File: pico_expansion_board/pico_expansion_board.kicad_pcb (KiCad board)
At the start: 4 copper layers, 99.1 x 69.8 mm, 55 parts, among them J1 DC12V/24V, J10 CAN_L, J2 TMC2209 Motor 1, J3 TMC2209 Motor 2, J4 Motor 1, J5 Motor 2, J6 A&D FX DB9_INV, J7 A&D FX DB9, J8 EXP1, J9 EXP2, SW1 SW_Push, U1 MAX232, U2 MCP2542FDxMF, U3 Pico, U4 AT24CS08-XHM, U5 TPS5450DDAR

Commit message: Update design
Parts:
- removed C10, C11: 4.7uF, Capacitor_SMD:C_0805_2012Metric
- removed C12, C13, C15: 0.01uF, Capacitor_SMD:C_0805_2012Metric
- removed C14: 220uF, Capacitor_SMD:CP_Elec_10x10.5
- removed D3: SS54, SnapEDAFootPrint:DO-214AC
- removed JP5: TX_OP2, Connector_PinHeader_2.54mm:PinHeader_1x02_P2.54mm_Vertical
- removed JP6: RX_OP2, Connector_PinHeader_2.54mm:PinHeader_1x02_P2.54mm_Vertical
- removed JP7: TX_OP1, Connector_PinHeader_2.54mm:PinHeader_1x02_P2.54mm_Vertical
- removed JP8: RX_OP1, Connector_PinHeader_2.54mm:PinHeader_1x02_P2.54mm_Vertical
- removed L2: 15uH, Inductor_SMD:L_Vishay_IHLP-4040
- removed R4: 10K, Resistor_SMD:R_0805_2012Metric
- removed R5: 3.16K, Resistor_SMD:R_0805_2012Metric
- removed TP3: TestPoint, TestPoint:TestPoint_Pad_2.0x2.0mm
- removed U5: TPS5450DDAR, SnapEDAFootPrint:CONV_TPS5450DDAR
- added C16: 10nF, Capacitor_SMD:C_0805_2012Metric, F.Cu at (130.0, 113.5)
- added C17: 10nF, Capacitor_SMD:C_0805_2012Metric, F.Cu at (120.1, 108.2)
- added C18: 330uF, Capacitor_SMD:CP_Elec_10x10.5, F.Cu at (115.3, 101.3)
- added C19: 10nF, Capacitor_SMD:C_0805_2012Metric, F.Cu at (125.0, 96.8)
- added C5: 4.7uF, Capacitor_SMD:C_0805_2012Metric, F.Cu at (124.5, 113.5)
- added C9: 4.7uF, Capacitor_SMD:C_0805_2012Metric, F.Cu at (127.3, 113.5)
- added D1: SS54, Extra Footprints:DO-214AC, F.Cu at (114.8, 108.2)
- added IC1: TPS5450DDA, Extra Footprints:SOIC127P600X170-9N, F.Cu at (119.1, 112.5)
- added L1: 15uH, Inductor_SMD:L_10.4x10.4_H4.8, F.Cu at (128.8, 104.9)
- added R2: 10K, Resistor_SMD:R_0805_2012Metric, F.Cu at (111.8, 112.3)
- added R6: 3.16K, Resistor_SMD:R_0805_2012Metric, F.Cu at (114.0, 112.3)
- added TP6: TestPoint, TestPoint:TestPoint_Pad_2.0x2.0mm, F.Cu at (133.9, 116.1)
- C2, C3: value 0.1uF -> 100nF
- C4: value 0.1uF -> 1uF
- H1, H2, H3, H4: footprint MountingHole:MountingHole_3.2mm_M3_Pad_Via -> MountingHole:MountingHole_3.2mm_M3_Pad
- J6: value A&D FX DB9_INV -> Straight Through
- J7: value A&D FX DB9 -> NULL Modem
- JP1, JP2: footprint Connector_PinHeader_2.54mm:PinHeader_1x02_P2.54mm_Vertical -> Connector_PinHeader_2.00mm:PinHeader_1x02_P2.00mm_Vertical
- JP3, JP4: footprint Connector_PinHeader_2.54mm:PinHeader_1x02_P2.54mm_Vertical -> Connector_PinSocket_2.00mm:PinSocket_1x02_P2.00mm_Vertical
- JP9: value TX_OP2 -> 120JP; footprint Connector_PinHeader_2.54mm:PinHeader_1x02_P2.54mm_Vertical -> Connector_PinHeader_2.00mm:PinHeader_1x02_P2.00mm_Vertical
- R1: value 10K -> 120Ω
- moved TP2 5.80 mm to (129.3, 86.1)
- moved TP8 3.07 mm to (68.8, 63.8)
- moved TP7 1.98 mm to (74.9, 63.8)
- moved TP1 1.21 mm to (129.3, 80.8), turned to -90 degrees
- moved JP2 0.52 mm to (70.3, 78.7)
- moved JP4 0.52 mm to (70.3, 105.9)
- moved JP9 0.36 mm to (114.6, 73.4)
- moved TP5 0.25 mm to (89.2, 102.9)
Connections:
- J6 pad 2: Net-(JP5-B) -> SCALE_RXD
- J6 pad 3: Net-(JP6-A) -> SCALE_TXD
- J7 pad 2: Net-(JP7-B) -> SCALE_TXD
- J7 pad 3: Net-(JP8-A) -> SCALE_RXD
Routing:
- net SCALE_TXD: track 19.5 -> 55.7 mm
- net Net-(JP6-A): track 28.8 -> 0.00 mm
- net Net-(JP5-B): track 28.5 -> 0.00 mm
- net SCALE_RXD: track 34.1 -> 57.0 mm, vias 2 -> 1
- net Net-(U5-PH): track 17.8 -> 0.00 mm
- net Net-(IC1-PH): track 0.00 -> 15.9 mm
- net Net-(JP8-A): track 11.4 -> 0.00 mm
- net Net-(JP7-B): track 10.6 -> 0.00 mm
- net +5V: track 36.8 -> 44.3 mm
- net CAN_TX: track 18.4 -> 12.2 mm, vias 0 -> 1
- net CAN_RX: track 17.8 -> 12.3 mm
- net Net-(IC1-VSENSE): track 0.00 -> 5.17 mm
- net Net-(U5-VSENSE): track 5.13 -> 0.00 mm
- net Net-(IC1-BOOT): track 0.00 -> 4.26 mm
- net Net-(U5-BOOT): track 4.13 -> 0.00 mm
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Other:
- board text added: "120Ω"
- board text added: "CAN-FD"
- board text added: "DCIN GND"
- board text added: "EXP1"
- board text added: "EXP2"
- board text added: "GND DCIN"
- board text added: "H L"
- board text added: "Motor 1 ADDR 0"
- board text added: "Motor 2 ADDR 1"
- board text added: "NULL Modem"
- board text added: "OpenTricker Controller v0.1"
- board text added: "PDN/UART"
- board text added: "RESET"
- board text added: "Raspberry Pi Pico"
- board text added: "Straight Through"

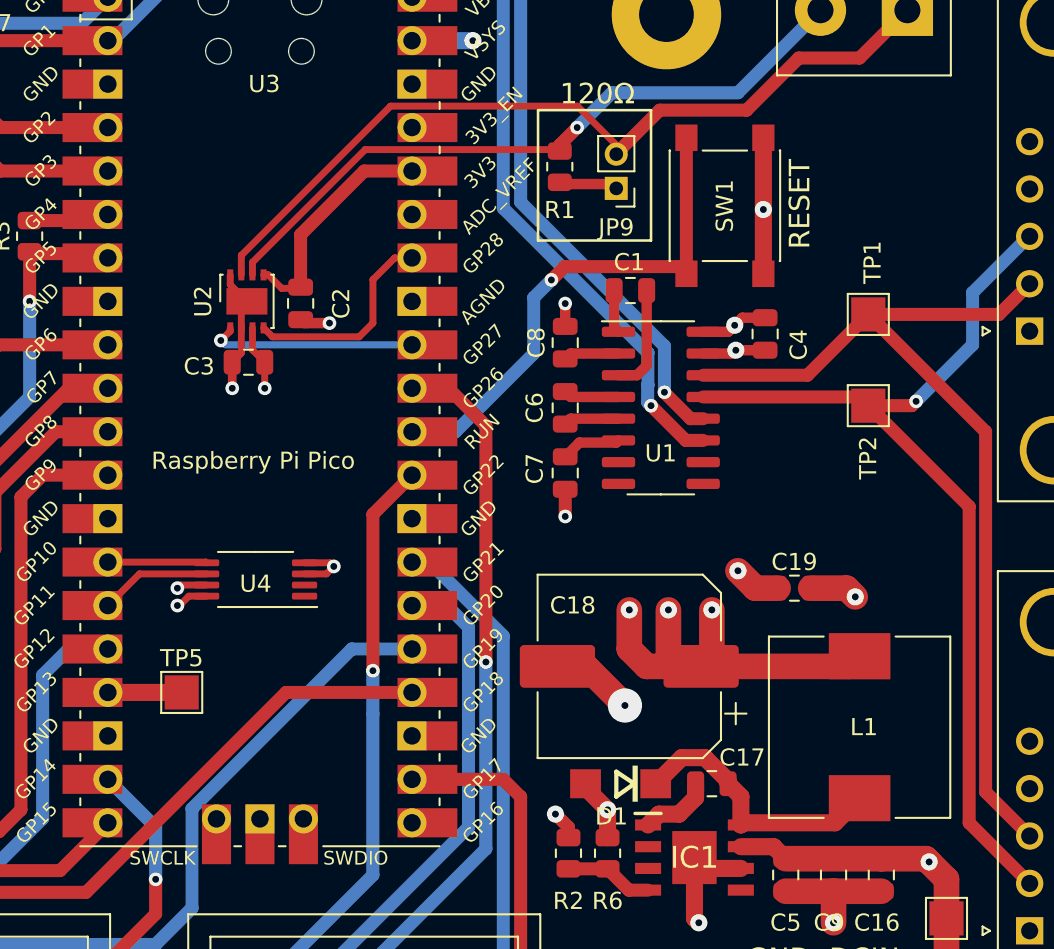
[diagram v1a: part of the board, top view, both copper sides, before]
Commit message: Add 3d models for pico and stepper drivers
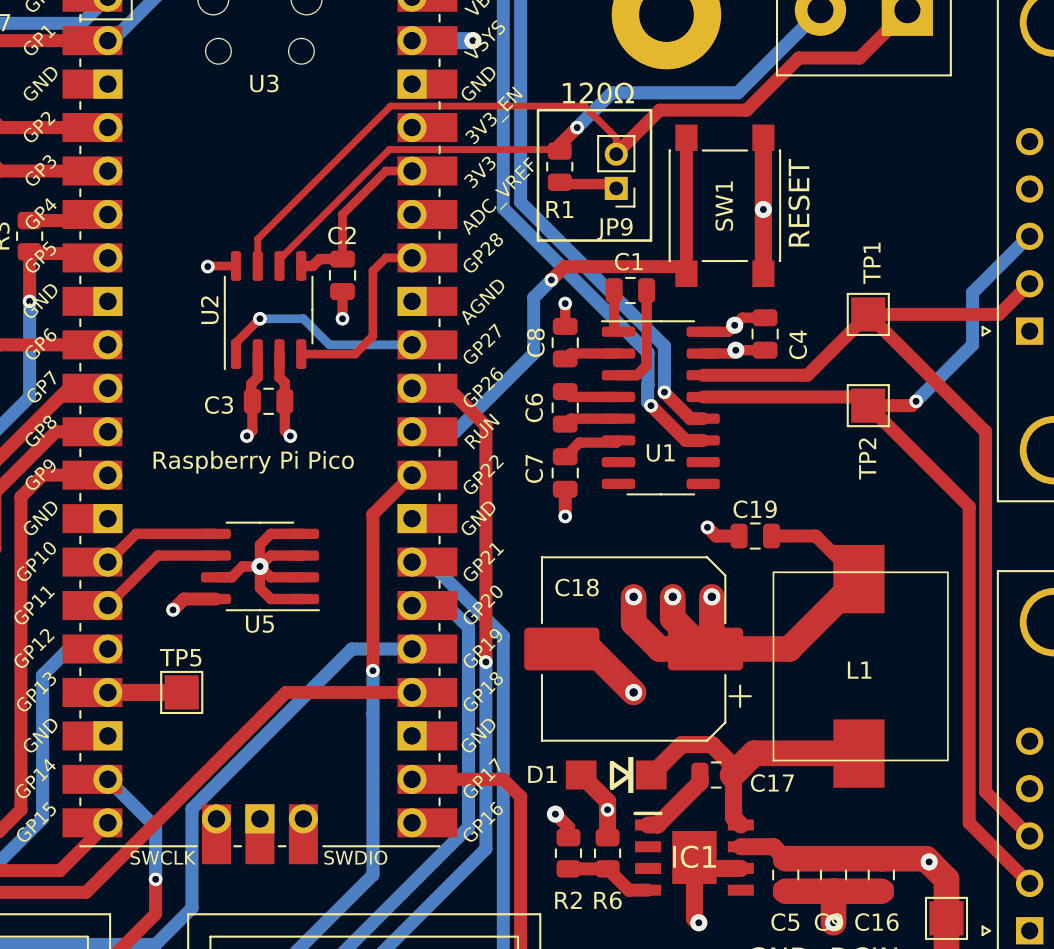
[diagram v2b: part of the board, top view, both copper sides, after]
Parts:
- removed U4: AT24CS08-XHM, Package_SO:TSSOP-8_4.4x3mm_P0.65mm
- added U5: CAT24C256, Package_SO:SO-8_3.9x4.9mm_P1.27mm, F.Cu at (93.7, 95.5)
- L1: footprint Inductor_SMD:L_10.4x10.4_H4.8 -> Extra Footprints:Power Inductor 10x11
- U2: footprint Package_DFN_QFN:DFN-8-1EP_3x3mm_P0.65mm_EP1.55x2.4mm -> Package_SO:SO-8_3.9x4.9mm_P1.27mm
- moved L1 5.40 mm to (123.7, 106.8)
- moved C19 3.81 mm to (122.7, 93.7)
- moved C2 2.95 mm to (98.6, 78.5)
- moved C3 2.57 mm to (94.2, 85.9)
- moved U2 1.37 mm to (94.2, 80.5)
- moved C18 1.05 mm to (115.6, 100.3)
- moved C17 0.57 mm to (120.4, 107.7)
- moved D1 0.57 mm to (114.6, 107.7)
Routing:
- net GND: track 53.5 -> 64.3 mm
- net +5V: track 44.3 -> 48.7 mm, vias 10 -> 9
- net +3.3V: track 13.6 -> 10.3 mm
- net Net-(J10-Pin_2): track 40.3 -> 38.3 mm
- net Net-(IC1-PH): track 15.9 -> 17.6 mm
- net CAN_RX: track 12.3 -> 11.0 mm
- net EEPROM_SDA: track 5.79 -> 7.00 mm
- net EEPROM_SCL: track 6.54 -> 7.52 mm
- net Net-(J10-Pin_1): track 48.7 -> 48.0 mm
